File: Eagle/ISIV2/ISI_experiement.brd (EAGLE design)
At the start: 100 x 81.7 mm, 59 parts, among them IC1 74AC11374D, IC3 74AC11374D, IC4 74AC11374D, IC5 74266D, IC6 74266D, IC7 74HC04D

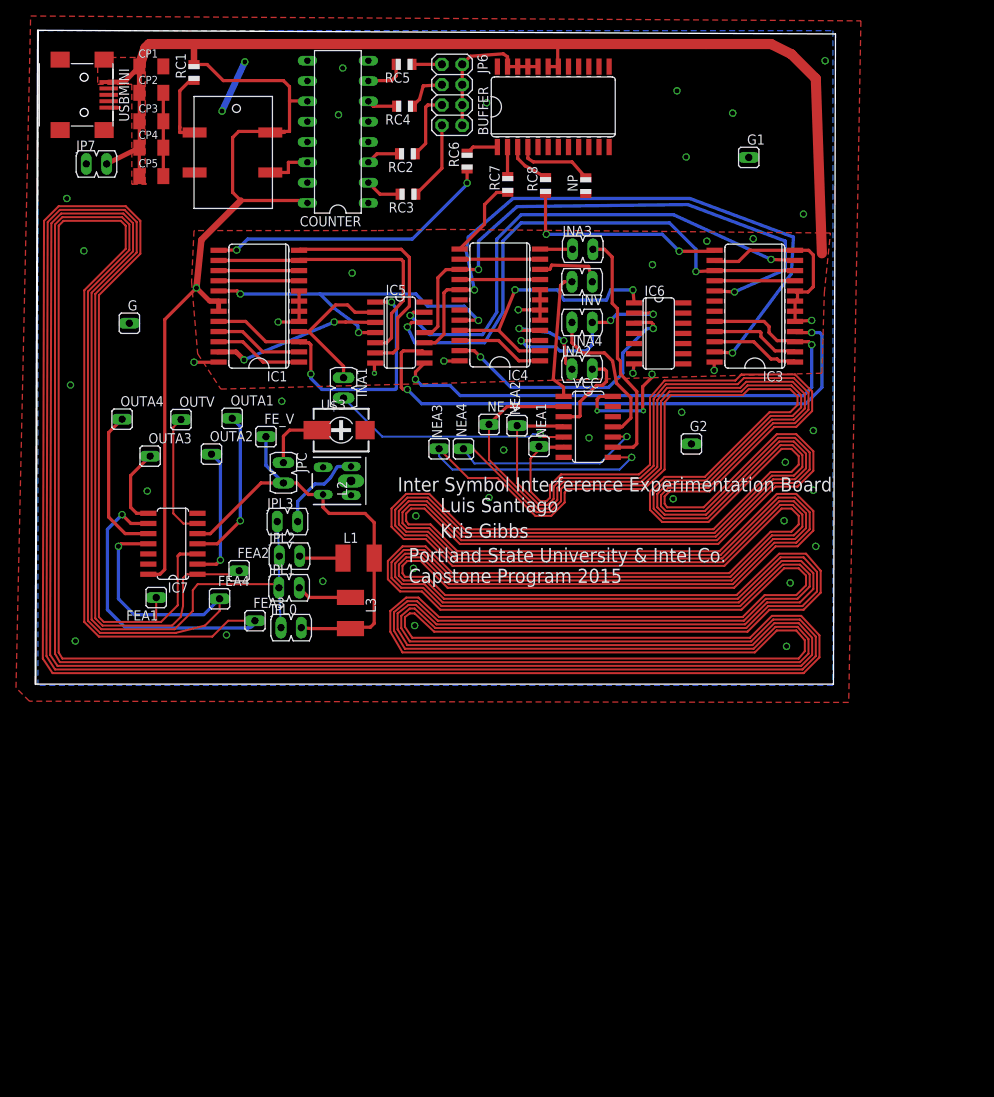
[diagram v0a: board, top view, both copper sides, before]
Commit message: ISI with test points
added test point to near and far end of TL
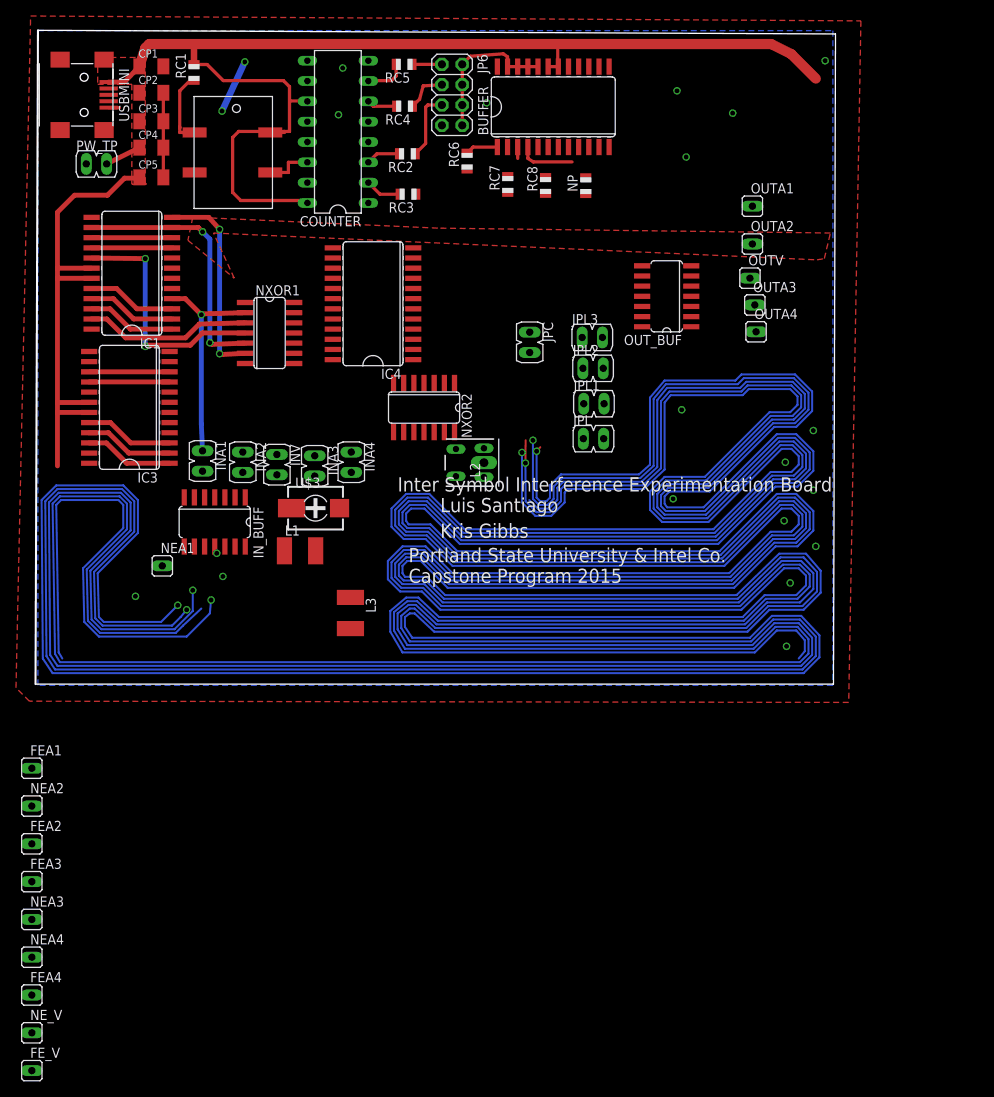
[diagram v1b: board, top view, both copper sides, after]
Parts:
- removed G, G1, G2: JP1, E3VB_ISI:JP1
- removed IC5, IC6: 74266D, 74xx-us:SO14
- removed IC7, VCC: 74HC04D, 74xx-eu:SO14
- removed JPL0: (no value), jumper:JP1
- added IN_BUFF, OUT_BUF: 74HC04D, 74xx-eu:SO14
- added JPL: (no value), jumper:JP1
- added NXOR1, NXOR2: 74266D, 74xx-us:SO14
- moved NE_V 95.1 mm to (-0.46, -43.6)
- moved FE_V 84.5 mm to (-0.46, -48.3)
- moved NEA4 83.4 mm to (-0.46, -34.1)
- moved OUTA4 80.0 mm to (90.1, 44.0)
- moved IC3 79.2 mm to (11.7, 34.6)
- moved OUTA3 77.9 mm to (89.9, 47.4)
- moved NEA3 77.8 mm to (-0.46, -29.4)
- moved NEA2 77.1 mm to (-0.46, -15.2)
- moved OUTV 73.3 mm to (89.3, 50.7)
- moved OUTA2 72.5 mm to (89.6, 55.0)
- moved OUTA1 70.2 mm to (89.6, 59.7)
- moved FEA4 54.8 mm to (-0.46, -38.9)
- moved NEA1 49.4 mm to (15.8, 14.8), turned to 0 degrees
- moved JPL2 44.6 mm to (69.7, 39.5)
- moved JPL3 44.5 mm to (69.6, 43.3)
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- renumbered JP7 to PW_TP
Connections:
- removed net N$13: IC7.4, OUTA1.1
- new net N$9: OUTA1.1, OUT_BUF.4
- net 1: now also IN_BUFF.10, OUT_BUF.11; no longer IC7.11, VCC.10
- net 2: now also IN_BUFF.4, OUT_BUF.1; no longer IC7.1, VCC.4
- net 3: now also IN_BUFF.8, OUT_BUF.9; no longer IC7.9, VCC.8
- net 4: now also IN_BUFF.6, OUT_BUF.3; no longer IC7.3, VCC.6
- net A2: now also NXOR1.8; no longer IC5.8
- net A5: now also NXOR1.12; no longer IC5.12
- net B1: now also NXOR2.1; no longer IC6.1
- net FB0: now also NXOR1.3; no longer IC5.3
- net FB1: now also NXOR1.4; no longer IC5.4
- net FB2: now also NXOR1.10; no longer IC5.10
- net FB3: now also NXOR1.11; no longer IC5.11
- net FB4: now also NXOR2.3; no longer IC6.3
- net GND: now also IN_BUFF.7, NXOR1.7, NXOR2.7, OUT_BUF.7; no longer G.1, G1.1, G2.1, IC5.7, IC6.7, IC7.7, VCC.7
- net N$14: now also IN_BUFF.5; no longer VCC.5
- net N$17: now also OUT_BUF.6; no longer IC7.6
- net N$19: now also OUT_BUF.10; no longer IC7.10
- net N$2: now also IN_BUFF.3; no longer VCC.3
- net N$20: now also OUT_BUF.2; no longer IC7.2
- net N$21: now also IN_BUFF.11; no longer VCC.11
- net N$22: now also IN_BUFF.1; no longer VCC.1
- net N$25: now also IN_BUFF.9; no longer VCC.9
- net N$4: now also JPL.2, OUT_BUF.5; no longer IC7.5, JPL0.2
- net OUTA4: now also OUT_BUF.8; no longer IC7.8
- net O_LFSR1: now also NXOR1.6; no longer IC5.6
- net O_LFSR2: now also NXOR1.9; no longer IC5.9
- net O_LSFR3: now also NXOR1.13; no longer IC5.13
- net Q2: now also NXOR1.1; no longer IC5.1
- net Q6: now also NXOR1.5; no longer IC5.5
- net TT_A1: now also NXOR1.2; no longer IC5.2
- net TT_A4: now also NXOR2.2; no longer IC6.2
- net V1: now also IN_BUFF.2, JPL.1; no longer JPL0.1, VCC.2
- net VCC: now also IN_BUFF.14, NXOR1.14, NXOR2.14, OUT_BUF.14; no longer IC5.14, IC6.14, IC7.14, VCC.14
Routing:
- net 3: track 754.0 -> 516.7 mm
- net 1: track 735.6 -> 610.2 mm
- net V1: track 722.6 -> 606.4 mm, vias 0 -> 1
- net 2: track 702.2 -> 612.7 mm, vias 0 -> 2
- net 4: track 698.7 -> 612.9 mm, vias 0 -> 2
- net FB2: track 81.2 -> 0.00 mm, vias 2 -> 0
- net O_LFSR2: track 71.8 -> 0.00 mm, vias 2 -> 0
- net FB3: track 71.0 -> 0.00 mm, vias 2 -> 0
- net O_LSFR3: track 64.2 -> 0.00 mm, vias 2 -> 0
- net A2: track 72.4 -> 11.1 mm, vias 2 -> 0
- net A5: track 68.3 -> 10.1 mm, vias 2 -> 0
- net N$4: track 56.4 -> 0.24 mm
- net GND: track 66.3 -> 18.7 mm, vias 44 -> 20
- net VCC: track 258.2 -> 211.2 mm, vias 5 -> 0
- net CLK1: track 36.9 -> 0.00 mm, vias 2 -> 0
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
